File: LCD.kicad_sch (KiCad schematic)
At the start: 9 parts, among them J1 AFC07-S40ECA-00, J2 AFC07-S10ECC-00

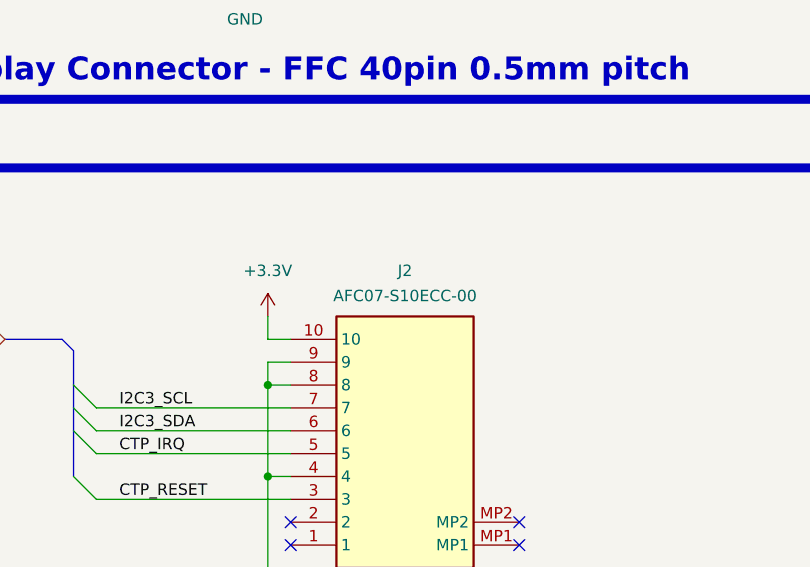
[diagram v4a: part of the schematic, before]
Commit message: update footprints, 3d models and layout
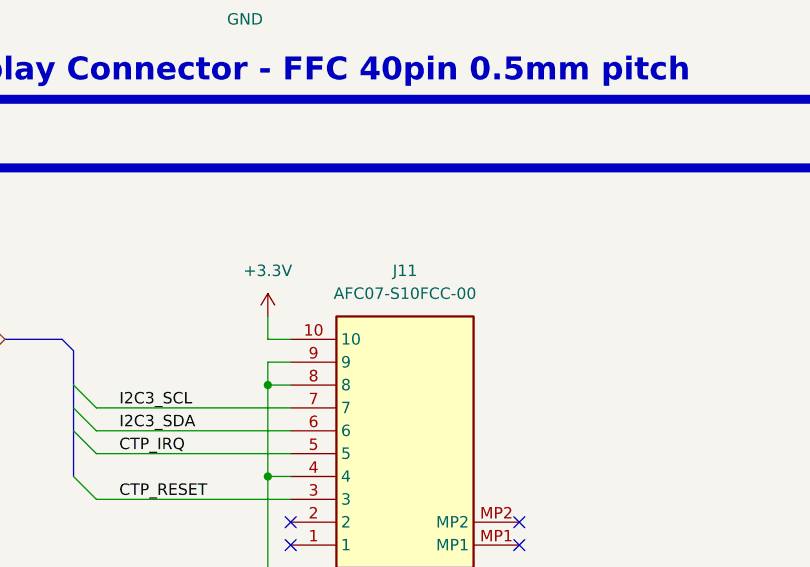
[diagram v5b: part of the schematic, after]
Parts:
- removed J2: AFC07-S10ECC-00, 0_connectors:AFC07S10ECC00, symbol 0_connectors:AFC07-S10ECC-00
- added J11: AFC07-S10FCC-00, 0_connectors:AFC07S10ECC00, symbol 0_connectors:AFC07-S10FCC-00 bottom contact
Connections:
- net +3.3V: now also J11.10
- net CTP_IRQ: now also J11.5
- net CTP_RESET: now also J11.3
- net GND: now also J11.4, J11.8, J11.9
- net I2C3_SCL: now also J11.7
- net I2C3_SDA: now also J11.6
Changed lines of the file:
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@@
 		)
 	)
-	(wire
-		(pts
-			(xy 224.79 203.2) (xy 246.38 203.2)
-		)
-		(stroke
-			(width 0)
-			(type default)
-		)
-	)
 	(bus
 		(pts
@@
 	(wire
 		(pts
+			(xy 224.79 193.04) (xy 246.38 193.04)
+		)
+		(stroke
+			(width 0)
+			(type default)
+		)
+	)
+	(wire
+		(pts
 			(xy 224.79 102.87) (xy 246.38 102.87)
 		)
@@
 	(wire
 		(pts
+			(xy 224.79 198.12) (xy 246.38 198.12)
+		)
+		(stroke
+			(width 0)
+			(type default)
+		)
+	)
+	(wire
+		(pts
 			(xy 224.79 39.37) (xy 246.38 39.37)
 		)
@@
 		)
 	)
-	(bus
+	(wire
 		(pts
-			(xy 222.25 186.69) (xy 220.98 185.42)
+			(xy 224.79 195.58) (xy 246.38 195.58)
 		)
 		(stroke
@@
 	(bus
 		(pts
-			(xy 222.25 97.79) (xy 222.25 100.33)
+			(xy 222.25 186.69) (xy 220.98 185.42)
 		)
 		(stroke
@@
 		)
 	)
-	(wire
+	(bus
 		(pts
-			(xy 224.79 193.04) (xy 246.38 193.04)
+			(xy 222.25 97.79) (xy 222.25 100.33)
 		)
 		(stroke
@@
 	(wire
 		(pts
+			(xy 224.79 203.2) (xy 246.38 203.2)
+		)
+		(stroke
+			(width 0)
+			(type default)
+		)
+	)
+	(wire
+		(pts
 			(xy 134.62 95.25) (xy 134.62 97.79)
 		)
@@
 		)
 	)
-	(wire
-		(pts
-			(xy 224.79 198.12) (xy 246.38 198.12)
-		)
-		(stroke
-			(width 0)
-			(type default)
-		)
-	)
 	(bus
 		(pts
@@
 	(wire
 		(pts
-			(xy 224.79 195.58) (xy 246.38 195.58)
-		)
-		(stroke
-			(width 0)
-			(type default)
-		)
-	)
-	(wire
-		(pts
 			(xy 243.84 182.88) (xy 243.84 185.42)
 		)
@@
 	)
 	(symbol
-		(lib_id "0_connectors:AFC07-S10ECC-00")
-		(at 271.78 208.28 180)
-		(unit 1)
-		(exclude_from_sim no)
-		(in_bom yes)
-		(on_board yes)
-		(dnp no)
-		(property "Reference" "J2"
-			(at 259.08 177.8 0)
-			(effects
-				(font
-					(size 1.27 1.27)
-				)
-			)
-		)
-		(property "Value" "AFC07-S10ECC-00"
-			(at 259.08 180.594 0)
-			(effects
-				(font
-					(size 1.27 1.27)
-				)
-			)
-		)
-		(property "Footprint" "0_connectors:AFC07S10ECC00"
-			(at 264.414 180.594 0)
-			(effects
-				(font
-					(size 1.27 1.27)
-				)
-				(justify left top)
-				(hide yes)
-			)
-		)
-		(property "Datasheet" "https://jlcpcb.com/api/file/downloadByFileSystemAccessId/8588894245574332416"
-			(at 250.19 13.36 0)
-			(effects
-				(font
-					(size 1.27 1.27)
-				)
-				(justify left top)
-				(hide yes)
-			)
-		)
-		(property "Description" "FFC, FPC Connectors 0.020\"0.50mm P=0.5mm RoHS"
-			(at 271.78 208.28 0)
-			(effects
-				(font
-					(size 1.27 1.27)
-				)
-				(hide yes)
-			)
-		)
-		(property "Height" "2"
-			(at 250.19 -186.64 0)
-			(effects
-				(font
-					(size 1.27 1.27)
-				)
-				(justify left top)
-				(hide yes)
-			)
-		)
-		(property "Manufacturer_Name" "JUSHUO"
-			(at 250.19 -286.64 0)
-			(effects
-				(font
-					(size 1.27 1.27)
-				)
-				(justify left top)
-				(hide yes)
-			)
-		)
-		(property "Manufacturer_Part_Number" "AFC07-S10ECC-00"
-			(at 250.19 -386.64 0)
-			(effects
-				(font
-					(size 1.27 1.27)
-				)
-				(justify left top)
-				(hide yes)
-			)
-		)
-		(property "Mouser Part Number" ""
-			(at 250.19 -486.64 0)
-			(effects
-				(font
-					(size 1.27 1.27)
-				)
-				(justify left top)
-				(hide yes)
-			)
-		)
-		(property "Mouser Price/Stock" ""
-			(at 250.19 -586.64 0)
-			(effects
-				(font
-					(size 1.27 1.27)
-				)
-				(justify left top)
-				(hide yes)
-			)
-		)
-		(property "Arrow Part Number" ""
-			(at 250.19 -686.64 0)
-			(effects
-				(font
-					(size 1.27 1.27)
-				)
-				(justify left top)
-				(hide yes)
-			)
-		)
-		(property "Arrow Price/Stock" ""
-			(at 250.19 -786.64 0)
-			(effects
-				(font
-					(size 1.27 1.27)
-				)
-				(justify left top)
-				(hide yes)
-			)
-		)
-		(property "Supplier 1" "JLCPCB"
-			(at 271.78 208.28 0)
-			(effects
-				(font
-					(size 1.27 1.27)
-				)
-				(hide yes)
-			)
-		)
-		(property "Supplier Part Number 1" "C262235"
-			(at 271.78 208.28 0)
-			(effects
-				(font
-					(size 1.27 1.27)
-				)
-				(hide yes)
-			)
-		)
-		(pin "6"
-		)
-		(pin "5"
-		)
-		(pin "2"
-		)
-		(pin "8"
-		)
-		(pin "4"
-		)
-		(pin "1"
-		)
-		(pin "9"
-		)
-		(pin "10"
-		)
-		(pin "MP1"
-		)
-		(pin "3"
-		)
-		(pin "7"
-		)
-		(pin "MP2"
-		)
-		(instances
-			(project ""
-				(path "/0650c7a8-acba-429c-9f8e-eec0baf0bc1c/fede4c36-00cc-4d3d-b71c-5243ba232202/5eacbcca-1b40-44c5-850e-98771545fbe2"
-					(reference "J2")
-					(unit 1)
-				)
-			)
-		)
-	)
-	(symbol
 		(lib_id "0_capacitors:CL05B104KO5NNNC")
 		(at 144.78 186.69 0)
@@
 					(unit 1)
 				)
+			)
+		)
+	)
+	(symbol
+		(lib_id "0_connectors:AFC07-S10FCC-00 bottom contact")
+		(at 271.78 208.28 180)
+		(unit 1)
+		(exclude_from_sim no)
+		(in_bom yes)
+		(on_board yes)
+		(dnp no)
+		(fields_autoplaced yes)
+		(property "Reference" "J11"
+			(at 259.08 177.8 0)
+			(effects
+				(font
+					(size 1.27 1.27)
+				)
+			)
+		)
+		(property "Value" "AFC07-S10FCC-00"
+			(at 259.08 180.34 0)
+			(effects
+				(font
+					(size 1.27 1.27)
+				)
+			)
+		)
+		(property "Footprint" "0_connectors:AFC07S10ECC00"
+			(at 264.414 180.594 0)
+			(effects
+				(font
+					(size 1.27 1.27)
+				)
+				(justify left top)
+				(hide yes)
+			)
+		)
+		(property "Datasheet" ""
+			(at 250.19 13.36 0)
+			(effects
+				(font
+					(size 1.27 1.27)
+				)
+				(justify left top)
+				(hide yes)
+			)
+		)
+		(property "Description" "FFC, FPC Connectors 0.020\"0.50mm P=0.5mm RoHS"
+			(at 271.78 208.28 0)
+			(effects
+				(font
+					(size 1.27 1.27)
+				)
+				(hide yes)
+			)
+		)
+		(property "Height" "2"
+			(at 250.19 -186.64 0)
+			(effects
+				(font
+					(size 1.27 1.27)
+				)
+				(justify left top)
+				(hide yes)
+			)
+		)
+		(property "Manufacturer_Name" "JUSHUO"
+			(at 250.19 -286.64 0)
+			(effects
+				(font
+					(size 1.27 1.27)
+				)
+				(justify left top)
+				(hide yes)
+			)
+		)
+		(property "Manufacturer_Part_Number" "AFC07-S10FCC-00 "
+			(at 250.19 -386.64 0)
+			(effects
+				(font
+					(size 1.27 1.27)
+				)
+				(justify left top)
+				(hide yes)
+			)
+		)
+		(property "Mouser Part Number" ""
+			(at 250.19 -486.64 0)
+			(effects
+				(font
+					(size 1.27 1.27)
+				)
+				(justify left top)
+				(hide yes)
+			)
+		)
+		(property "Mouser Price/Stock" ""
+			(at 250.19 -586.64 0)
+			(effects
+				(font
+					(size 1.27 1.27)
+				)
+				(justify left top)
+				(hide yes)
+			)
+		)
+		(property "Arrow Part Number" ""
+			(at 250.19 -686.64 0)
+			(effects
+				(font
+					(size 1.27 1.27)
+				)
+				(justify left top)
+				(hide yes)
+			)
+		)
+		(property "Arrow Price/Stock" ""
+			(at 250.19 -786.64 0)
+			(effects
+				(font
+					(size 1.27 1.27)
+				)
+				(justify left top)
+				(hide yes)
+			)
+		)
+		(property "Supplier 1" "JLCPCB"
+			(at 271.78 208.28 0)
+			(effects
+				(font
+					(size 1.27 1.27)
+				)
+				(hide yes)
+			)
+		)
+		(property "Supplier Part Number 1" "C11050"
+			(at 271.78 208.28 0)
+			(effects
+				(font
+					(size 1.27 1.27)
+				)
+				(hide yes)
+			)
+		)
+		(pin "7"
+		)
+		(pin "3"
+		)
+		(pin "1"
+		)
+		(pin "MP1"
+		)
+		(pin "6"
+		)
+		(pin "4"
+		)
+		(pin "9"
+		)
+		(pin "10"
+		)
+		(pin "MP2"
+		)
+		(pin "2"
+		)
+		(pin "5"
+		)
+		(pin "8"
+		)
+		(instances
+			(project "transmitter"
+				(path "/0650c7a8-acba-429c-9f8e-eec0baf0bc1c/fede4c36-00cc-4d3d-b71c-5243ba232202/5eacbcca-1b40-44c5-850e-98771545fbe2"
+					(reference "J11")
+					(unit 1)
+				)

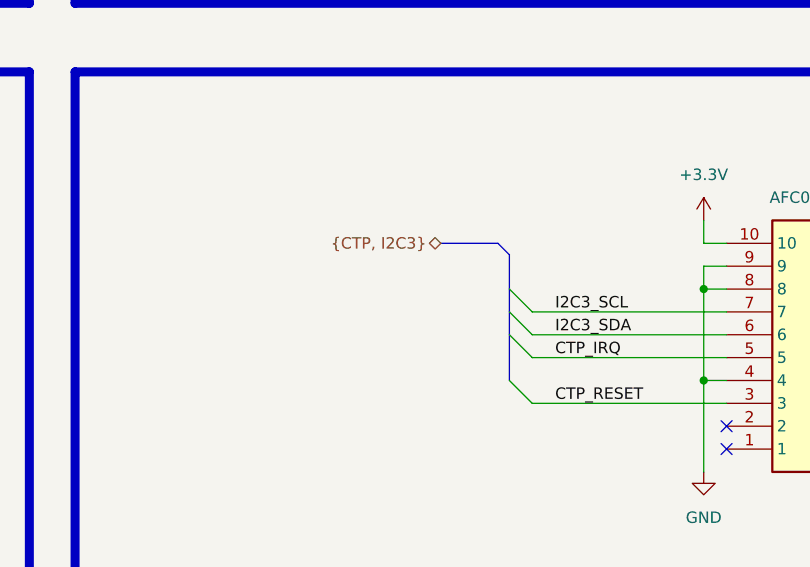
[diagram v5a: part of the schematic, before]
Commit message: qspi layout, length matching, sdcard lengthmatching, change some footprints, prototype production generation
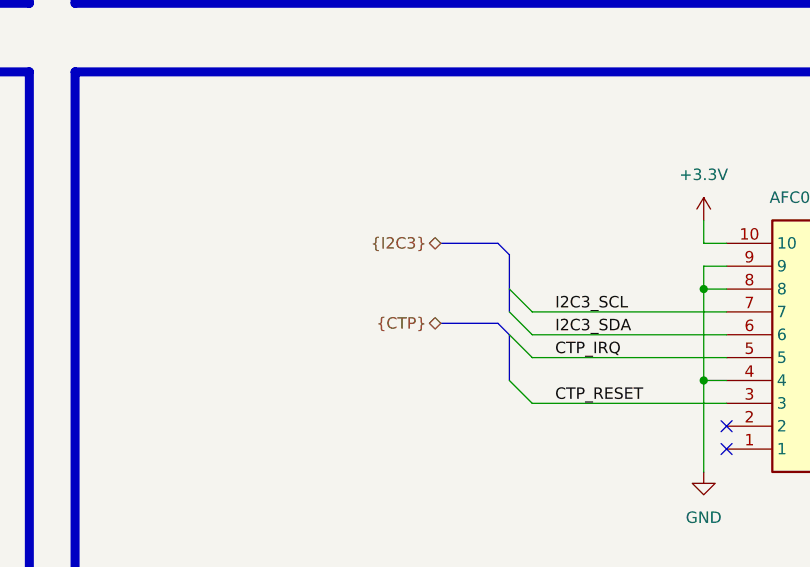
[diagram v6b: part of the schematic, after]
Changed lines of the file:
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@@
 		)
 	)
+	(bus
+		(pts
+			(xy 214.63 194.31) (xy 220.98 194.31)
+		)
+		(stroke
+			(width 0)
+			(type default)
+		)
+	)
 	(wire
 		(pts
@@
 		)
 	)
-	(bus
-		(pts
-			(xy 222.25 195.58) (xy 222.25 200.66)
-		)
-		(stroke
-			(width 0)
-			(type default)
-		)
-	)
 	(wire
 		(pts
@@
 		)
 	)
-	(bus
+	(wire
 		(pts
-			(xy 222.25 193.04) (xy 222.25 195.58)
+			(xy 224.79 118.11) (xy 246.38 118.11)
 		)
 		(stroke
@@
 	(wire
 		(pts
-			(xy 224.79 118.11) (xy 246.38 118.11)
+			(xy 243.84 200.66) (xy 243.84 210.82)
 		)
 		(stroke
@@
 	(wire
 		(pts
-			(xy 243.84 200.66) (xy 243.84 210.82)
+			(xy 224.79 77.47) (xy 246.38 77.47)
 		)
 		(stroke
@@
 	(wire
 		(pts
-			(xy 224.79 77.47) (xy 246.38 77.47)
+			(xy 224.79 105.41) (xy 246.38 105.41)
 		)
 		(stroke
@@
 		)
 	)
-	(wire
+	(bus
 		(pts
-			(xy 224.79 105.41) (xy 246.38 105.41)
+			(xy 222.25 195.58) (xy 222.25 200.66)
+		)
+		(stroke
+			(width 0)
+			(type default)
+		)
+	)
+	(bus
+		(pts
+			(xy 222.25 195.58) (xy 220.98 194.31)
 		)
 		(stroke
@@
 		)
 	)
-	(hierarchical_label "{CTP, I2C3}"
+	(hierarchical_label "{I2C3}"
 		(shape bidirectional)
 		(at 214.63 185.42 180)
 		(effects
 			(font
+				(size 1.27 1.27)
+			)
+			(justify right)
+		)
+	)
+	(hierarchical_label "{CTP}"
+		(shape bidirectional)
+		(at 214.63 194.31 180)
+		(effects
+			(font

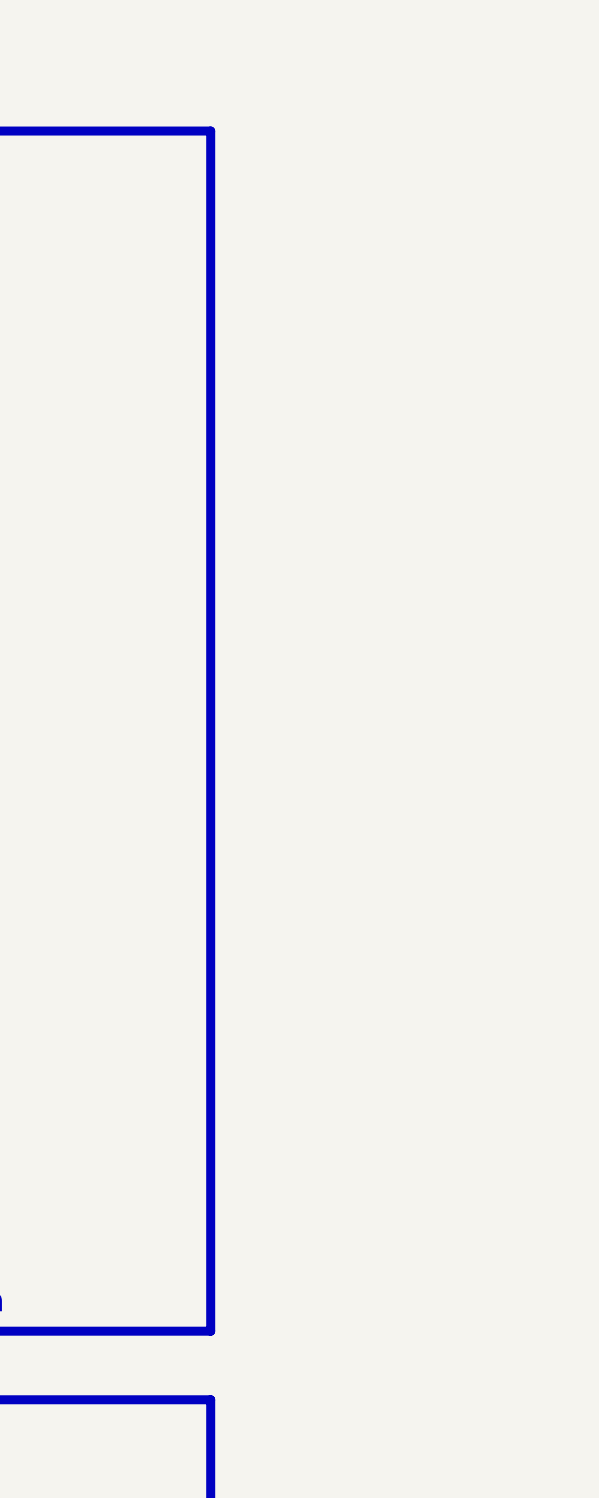
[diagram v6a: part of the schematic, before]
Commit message: added fiducal markers, mounting holes, testpoints
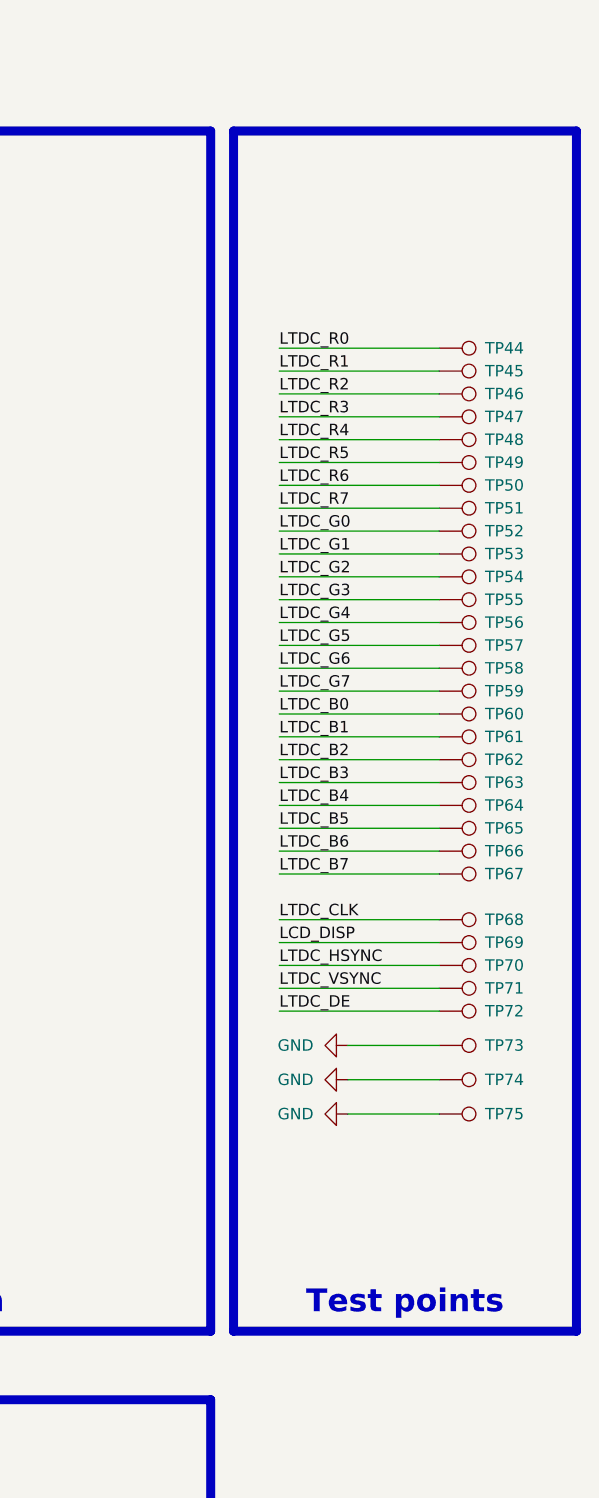
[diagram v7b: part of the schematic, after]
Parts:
- added TP44, TP45, TP46, TP47, TP48, TP49, TP50, TP51, TP52, TP53, TP54, TP55, TP56, TP57, TP58, TP59, TP60, TP61, TP62, TP63, TP64, TP65, TP66, TP67, TP68, TP69, TP70, TP71, TP72, TP73, TP74, TP75: TestPoint, 0_pads:TestPoint_Pad_D0.4mm_Back, symbol Connector:TestPoint
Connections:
- net GND: now also TP73.1, TP74.1, TP75.1
- net LCD_DISP: now also TP69.1
- net LTDC_B0: now also TP60.1
- net LTDC_B1: now also TP61.1
- net LTDC_B2: now also TP62.1
- net LTDC_B3: now also TP63.1
- net LTDC_B4: now also TP64.1
- net LTDC_B5: now also TP65.1
- net LTDC_B6: now also TP66.1
- net LTDC_B7: now also TP67.1
- net LTDC_CLK: now also TP68.1
- net LTDC_DE: now also TP72.1
- net LTDC_G0: now also TP52.1
- net LTDC_G1: now also TP53.1
- net LTDC_G2: now also TP54.1
- net LTDC_G3: now also TP55.1
- net LTDC_G4: now also TP56.1
- net LTDC_G5: now also TP57.1
- net LTDC_G6: now also TP58.1
- net LTDC_G7: now also TP59.1
- net LTDC_HSYNC: now also TP70.1
- net LTDC_R0: now also TP44.1
- net LTDC_R1: now also TP45.1
- net LTDC_R2: now also TP46.1
- net LTDC_R3: now also TP47.1
- net LTDC_R4: now also TP48.1
- net LTDC_R5: now also TP49.1
- net LTDC_R6: now also TP50.1
- net LTDC_R7: now also TP51.1
- net LTDC_VSYNC: now also TP71.1
